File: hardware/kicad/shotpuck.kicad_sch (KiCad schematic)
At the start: 34 parts, among them J1 Samzo PR5L4015-2P-C-F, J2 SWD pads, Q1 DMN63D8LDW, Q2 DMN2004DWK, U1 BMD-340-A-R, U2 LSM6DSO32TR, U3 MCP73831T-2ACI/OT, U4 BQ29700DSER

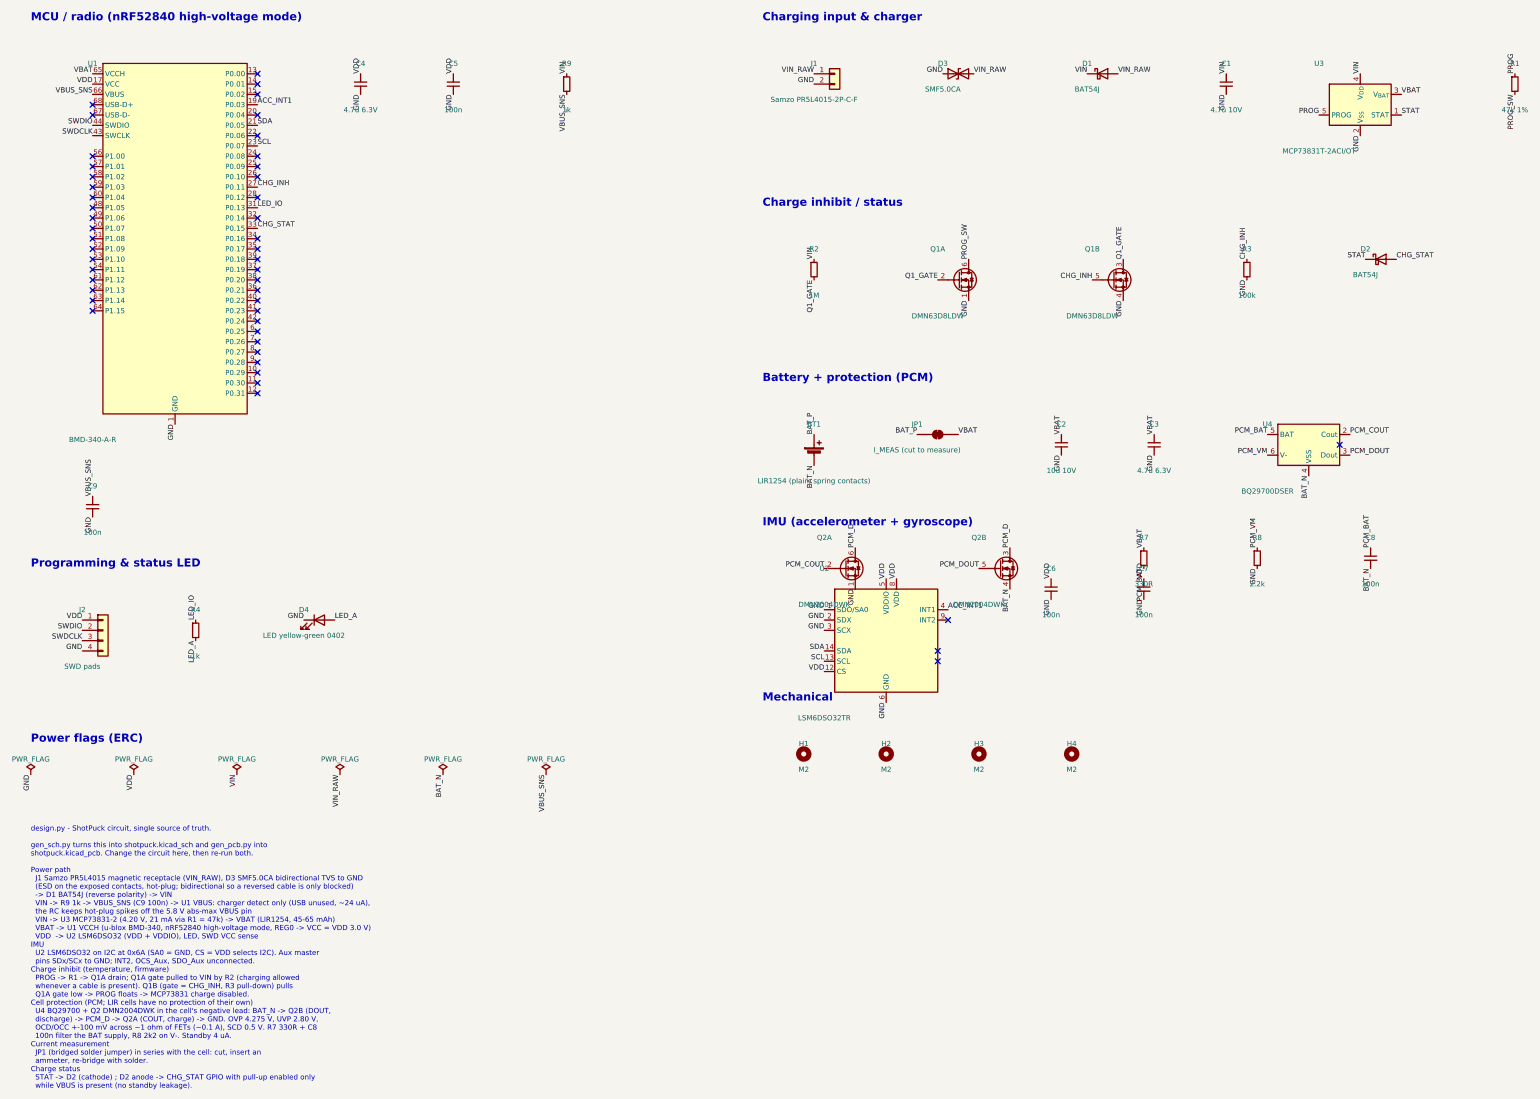
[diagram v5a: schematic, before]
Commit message: Add USB-C side-port board variant
- J1: side-mounted HRO TYPE-C-31-M-17 (6-pin, power only) replaces the
  magnetic Samzo connector; R10/R11 5.1k pull CC1/CC2 down. Footprint copy
  ShotPuck:..._NoFrontSilk drops the silkscreen outside the board edge.
- Module slid 45 deg around the sleeve; copper-free right side
  (board_shape.rf_keepout), IMU and its caps moved next to the module.
- Decoupling: C5 removed from board and schematic (the BMD-340 has 4.7 uF
  on VCC inside, C4 stays); C6/C7 moved next to IMU pins 8 and 5, C1 next
  to the charger input, vias moved out of U3's pads.
- BT1 uses ShotPuck:LIR1254_Contacts_Edit (pad 2 at 270 deg).
- Schematic: local power symbol ShotPuck:GND_LOCAL keeps the net /GND.
- DRC with zone refill: 0 errors, 0 unconnected, schematic parity clean.

design.py, gen_sch.py and gen_pcb.py still list C5, and gen_sch.py
rewrites ShotPuck.kicad_sym without GND_LOCAL: regenerating undoes the
hand edits.

Co-Authored-By: Claude Opus 5.5 <noreply@anthropic.com>
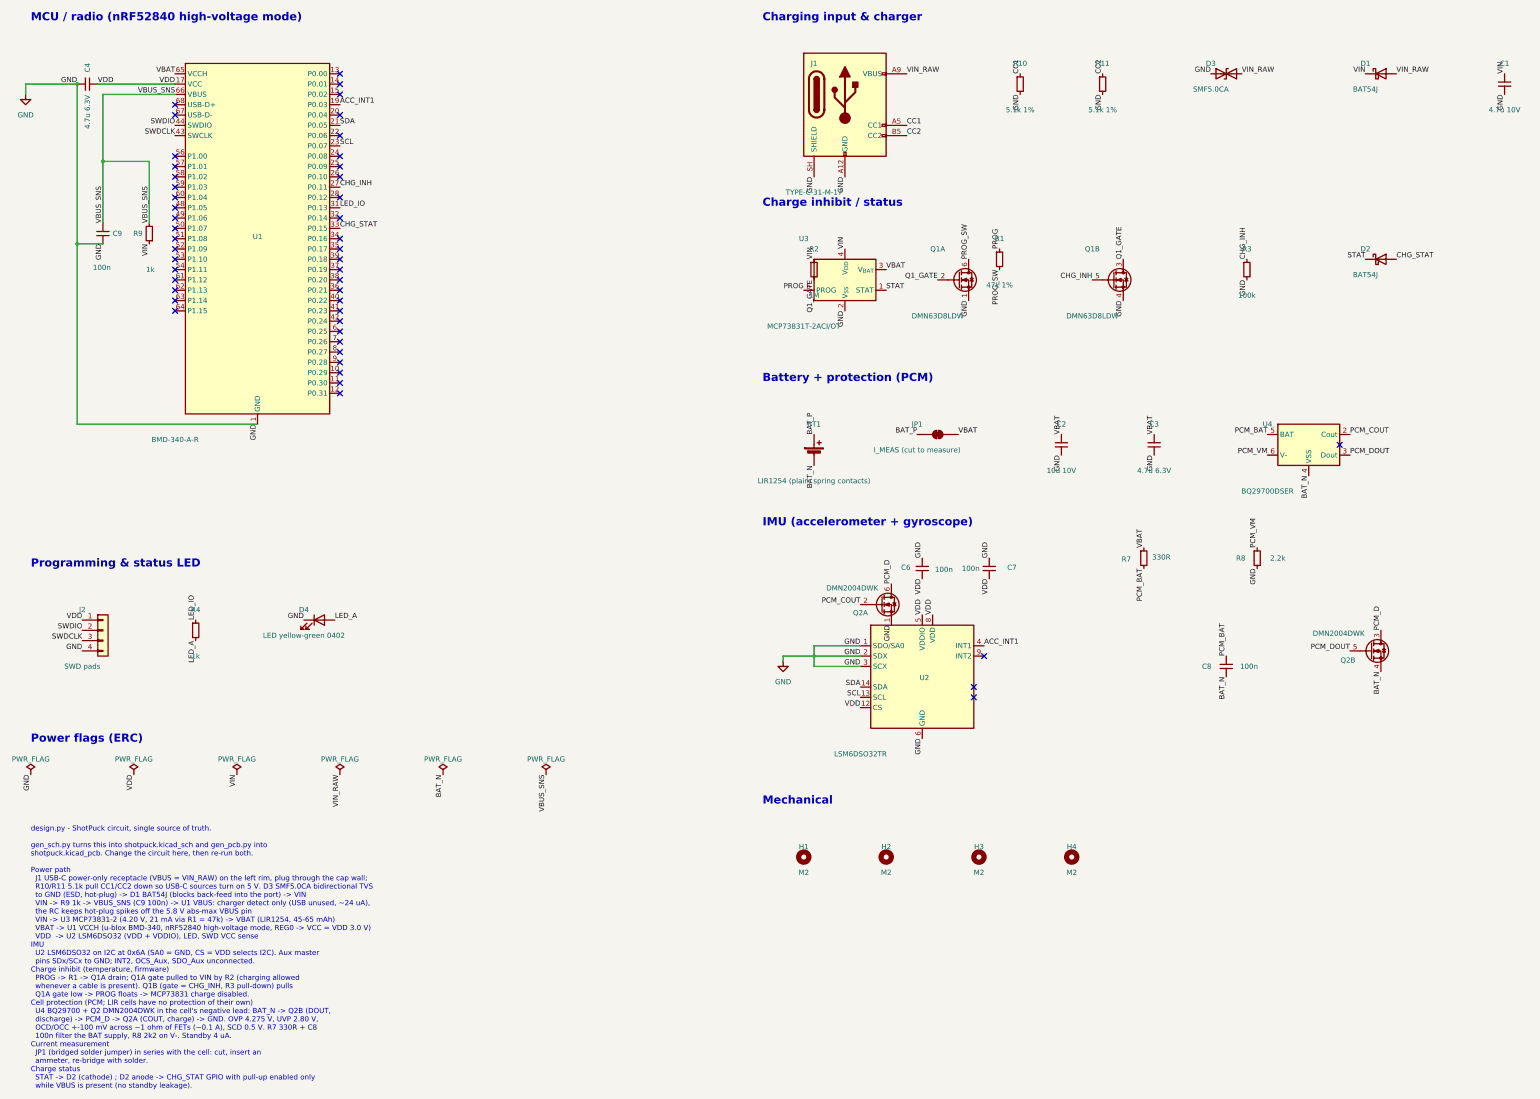
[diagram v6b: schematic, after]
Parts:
- removed C5: 100n, Capacitor_SMD:C_0402_1005Metric, symbol Device:C_Small
- added R10, R11: 5.1k 1%, Resistor_SMD:R_0402_1005Metric, symbol Device:R_Small
- BT1: footprint ShotPuck:LIR1254_Contacts -> ShotPuck:LIR1254_Contacts_Edit
- C1, C2, C3, C4, C6, C7, C8, C9, D4, R1, R2, R3, R4, R7, R8, R9: KiLib_Generator (none) -> SMD_2terminal_chip_molded
- J1: value Samzo PR5L4015-2P-C-F -> TYPE-C-31-M-17; footprint ShotPuck:MagPogo_Samzo_2P -> ShotPuck:USB_C_Receptacle_HRO_TYPE-C-31-M-17_NoFrontSilk; symbol Connector_Generic:Conn_01x02 -> Connector:USB_C_Receptacle_PowerOnly_6P
- Q1, Q2, U3: KiLib_Generator (none) -> package/gullwing
- U2: KiLib_Generator (none) -> package/no_lead
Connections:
- net GND: now also J1.A12 (GND), J1.B12 (GND), J1.SH (SHIELD), R10.2, R11.2; no longer J1.2 (Pin_2)
- net VIN_RAW: now also J1.A9 (VBUS), J1.B9 (VBUS); no longer J1.1 (Pin_1)
- new net CC1: J1.A5 (CC1), R10.1
- new net CC2: J1.B5 (CC2), R11.1
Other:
- note added: "design.py - ShotPuck circuit, single source of truth. gen_sch.py turns this into shotpuck.kicad_sch and gen_pcb.py into shotpuck.kicad_pcb. Change the circuit here, then re-run both. Power path J1 USB-C power-only receptacle (VBUS = VIN_RAW) on the left rim, plug through the cap wall; R10/R11 5.1k pull CC1/CC2 down so USB-C sources turn on 5 V. D3 SMF5.0CA bidirectional TVS to GND (ESD, hot-plug)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"
- note removed: "design.py - ShotPuck circuit, single source of truth. gen_sch.py turns this into shotpuck.kicad_sch and gen_pcb.py into shotpuck.kicad_pcb. Change the circuit here, then re-run both. Power path J1 Samzo PR5L4015 magnetic receptacle (VIN_RAW), D3 SMF5.0CA bidirectional TVS to GND (ESD on the exposed contacts, hot-plug; bidirectional so a reversed cable is only blocked) -> D1 BAT54J (reverse polari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"
- moved on the sheet: C1, C4, C6, C7, C8, C9, D1, D3, H1, H2, H3, H4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

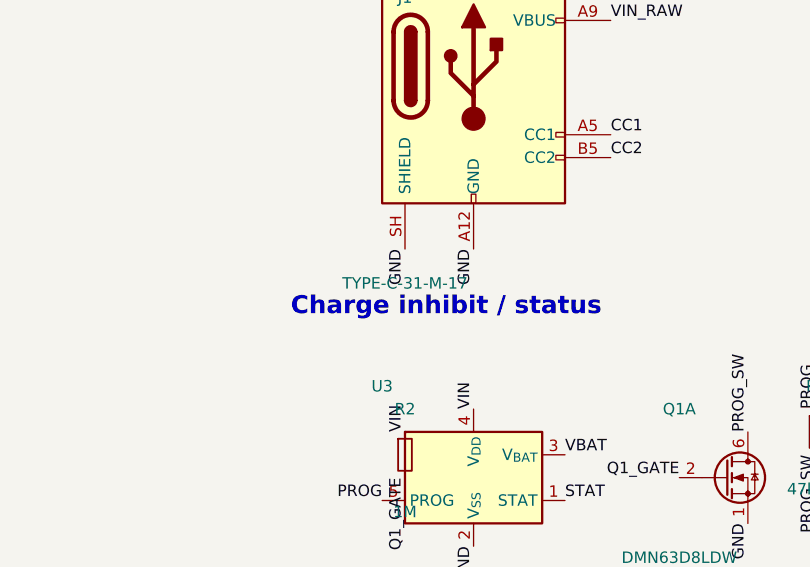
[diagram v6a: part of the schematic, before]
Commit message: Switch J1 to waterproof IPX8 USB-C (C3020041) and seal the cap
- J1: SHOU HAN TYPE-C 6PFS 2JCB1.6-H6.7 IPX8 (LCSC C3020041), recessed
  into a 10.28 x 5.22 mm notch in the board edge at 132.58 deg, midway
  between H1 and H2. Footprint from the datasheet drawing (pads kept
  0.3/0.35 mm from the notch; the notch sides run through two 0.70 mm
  NPTH holes for the legs, since the datasheet's 0.69 mm U-slots cannot
  be routed); LCSC's STEP model shifted -1.93 mm onto the pads.
- H1/H2 moved apart so the ground pour reaches the wing tabs; layout.json
  bosses follow (plate holes, cap bosses, standoffs).
- GND via at (-0.41, 16.09): the pour around U2's GND pins 6/7 reached
  the rest of GND only along the rim, where the top tab's mouse bites cut
  it.
- Cap: the silicone ring seals in an obround hole in the wall (0.15 mm
  squeeze per side), a flat at the receptacle face lets any compliant
  plug seat fully, a pocket over the body leaves 0.67 mm of cap top.
  CadQuery check with the real STEP model: only the ring squeeze
  overlaps; a maximum-size plug overmold clears cap and plate.
- Panel: 2 mm backbone between the rows, top tab 1.5 mm wide at 86 deg
  (clear of H1 and the via at 80 deg); panel 91.1 x 92.7 mm.
- gen_panel.py places tabs from the board's own centre (the board sits at
  (132.06, 91.40) on the KiCad page); the Blender GLB export uses the
  same origin and takes J1 from the board.
- Board DRC 0/0 with schematic parity; panel DRC 0/0; BOM/CPL/Gerbers
  regenerated.

mechanical/out/shotpuck_assembly.mp4 and .blend are from the render
before the waterproof port and still show the earlier cap; re-render
with mechanical/blender/render_assembly.py. gen_pcb.py does not draw
the port notch, and design.py still lists C5.

Co-Authored-By: Claude Opus 5.5 <noreply@anthropic.com>
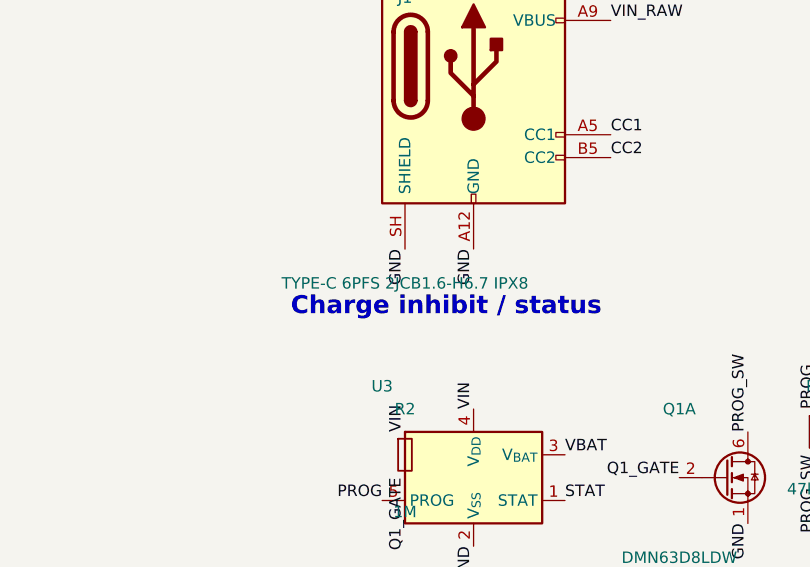
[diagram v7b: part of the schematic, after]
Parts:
- J1: value TYPE-C-31-M-17 -> TYPE-C 6PFS 2JCB1.6-H6.7 IPX8; footprint ShotPuck:USB_C_Receptacle_HRO_TYPE-C-31-M-17_NoFrontSilk -> ShotPuck:USB_C_Receptacle_ShouHan_TYPE-C-6PFS-2JCB1.6-H6.7_IPX8
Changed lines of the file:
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@@
 			)
 		)
-		(property "Value" "TYPE-C-31-M-17"
+		(property "Value" "TYPE-C 6PFS 2JCB1.6-H6.7 IPX8"
 			(at 215.9 72.39 0)
 			(show_name no)
@@
 			)
 		)
-		(property "Footprint" "ShotPuck:USB_C_Receptacle_HRO_TYPE-C-31-M-17_NoFrontSilk"
+		(property "Footprint" "ShotPuck:USB_C_Receptacle_ShouHan_TYPE-C-6PFS-2JCB1.6-H6.7_IPX8"
 			(at 223.52 50.8 0)
 			(hide yes)
@@
 			)
 		)
-		(property "Datasheet" ""
+		(property "Datasheet" "https://wmsc.lcsc.com/wmsc/upload/file/pdf/v2/lcsc/2205231645_SHOU-HAN-TYPE-C-6PFS-2JCB1-6-H6-7-IPX8_C3020041.pdf"
 			(at 223.52 50.8 0)
 			(hide yes)

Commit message: Add charger LED, JP2 reset pads and firmware recovery (0.2.1)
Charger LED: one blink every 2 s while charging, steady once the charger
has terminated (so the LED never holds off termination), three blinks
when the temperature gate pauses charging.

JP2: two bare round pads (0.8 mm, 0.4 mm gap) on module pin 7 (P0.26)
and GND. With the cap off, bridging them for 5 s erases settings,
pairings, shot count and log and reboots; only a bridge made while
running counts. Three crash or watchdog resets in a row, each within a
minute of boot, erase the same data automatically. A trial OTA image is
now confirmed only after a paired phone connects over an encrypted link.

Firmware rebuilt and signed as 0.2.1; panel gerbers and JLC BOM/CPL
regenerated (JP2 is copper only).

Co-Authored-By: Claude Opus 5.5 <noreply@anthropic.com>
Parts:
- added JP2: RESET pads, ShotPuck:TweezerPads_2x0.8mm_Gap0.4mm, symbol Jumper:SolderJumper_2_Open
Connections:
- net GND: now also JP2.2 (B)
- net BTN: now reaches U1.7 (P0.26)
- net BTN: now also JP2.1 (A)
- no-connect marks 48 -> 47
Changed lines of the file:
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@@
 	)
 	(no_connect
-		(at 99.06 109.22)
+		(at 99.06 86.36)
 	)
 	(no_connect
@@
 	(no_connect
 		(at 345.44 134.62)
-	)
-	(no_connect
-		(at 99.06 86.36)
 	)
 	(no_connect
@@
 			(width 0)
 			(type default)
+		)
+	)
+	(label "BTN"
+		(at 99.06 109.22 0)
+		(effects
+			(font
+				(size 1.27 1.27)
+			)
+			(justify left bottom)
+		)
+	)
+	(label "BTN"
+		(at 125.73 177.8 180)
+		(effects
+			(font
+				(size 1.27 1.27)
+			)
+			(justify right bottom)
+		)
+	)
+	(label "GND"
+		(at 135.89 177.8 0)
+		(effects
+			(font
+				(size 1.27 1.27)
+			)
+			(justify left bottom)
 		)
 	)
@@
 					(unit 1)
 				)
+			)
+		)
+	)
+	(symbol
+		(lib_id "Jumper:SolderJumper_2_Open")
+		(at 130.81 177.8 0)
+		(unit 1)
+		(body_style 1)
+		(exclude_from_sim no)
+		(in_bom yes)
+		(on_board yes)
+		(in_pos_files yes)
+		(dnp no)
+		(property "Reference" "JP2"
+			(at 130.81 173.99 0)
+			(show_name no)
+			(do_not_autoplace no)
+			(effects
+				(font
+					(size 1.27 1.27)
+				)
+			)
+		)
+		(property "Value" "RESET pads"
+			(at 130.81 181.61 0)
+			(show_name no)
+			(do_not_autoplace no)
+			(effects
+				(font
+					(size 1.27 1.27)
+				)
+			)
+		)
+		(property "Footprint" "ShotPuck:TweezerPads_2x0.8mm_Gap0.4mm"
+			(at 130.81 177.8 0)
+			(hide yes)
+			(show_name no)
+			(do_not_autoplace no)
+			(effects
+				(font
+					(size 1.27 1.27)
+				)
+			)
+		)
+		(property "Datasheet" ""
+			(at 130.81 177.8 0)
+			(hide yes)
+			(show_name no)
+			(do_not_autoplace no)
+			(effects
+				(font
+					(size 1.27 1.27)
+				)
+			)
+		)
+		(property "Description" "Bridge with tweezers (cap off) for a factory reset"
+			(at 130.81 177.8 0)
+			(hide yes)
+			(show_name no)
+			(do_not_autoplace no)
+			(effects
+				(font
+					(size 1.27 1.27)
+				)
+			)
+		)
+		(pin "1"
+		)
+		(pin "2"
+		)
+		(instances
+			(project "shotpuck"
+				(path "/453e4d2c-678b-52c6-881c-d1e900c8fc33"
+					(reference "JP2")
+					(unit 1)
+				)
